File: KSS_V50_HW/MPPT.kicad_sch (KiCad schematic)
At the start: 33 parts, among them Q5 DMG3414U-7, U1 SPV1040, U2 INA236

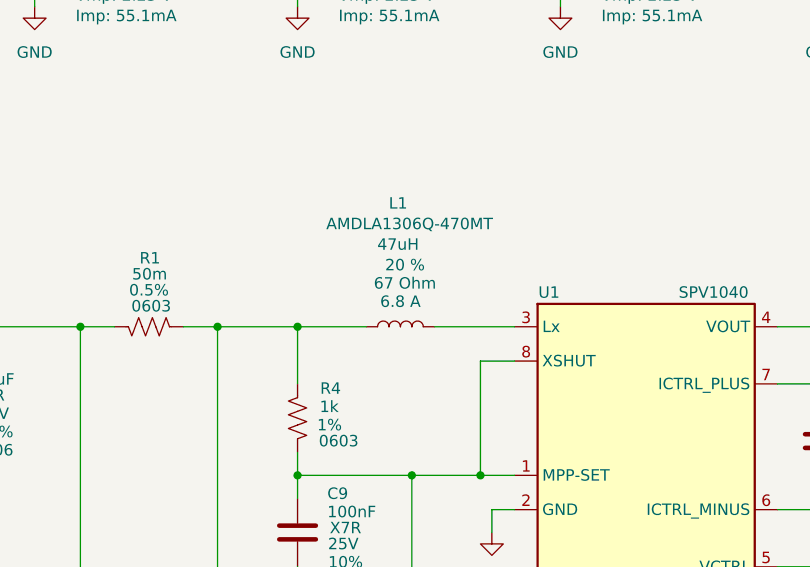
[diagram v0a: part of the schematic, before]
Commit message: minor changed based on Wilson's first review and personal layout round
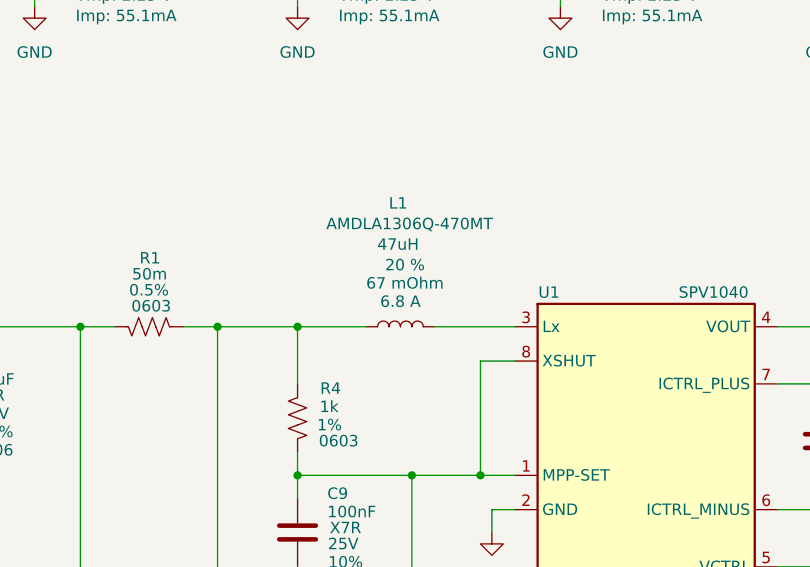
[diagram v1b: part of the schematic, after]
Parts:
- L1: DCR 67 Ohm -> 67 mOhm
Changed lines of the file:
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@@
 			)
 		)
-		(property "DCR" "67 Ohm"
+		(property "DCR" "67 mOhm"
 			(at 128.778 84.074 90)
 			(effects
